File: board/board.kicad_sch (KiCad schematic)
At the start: 5 parts, among them J1 022_battery_cells, J2 Conn_01x02_Male, J3 003_power

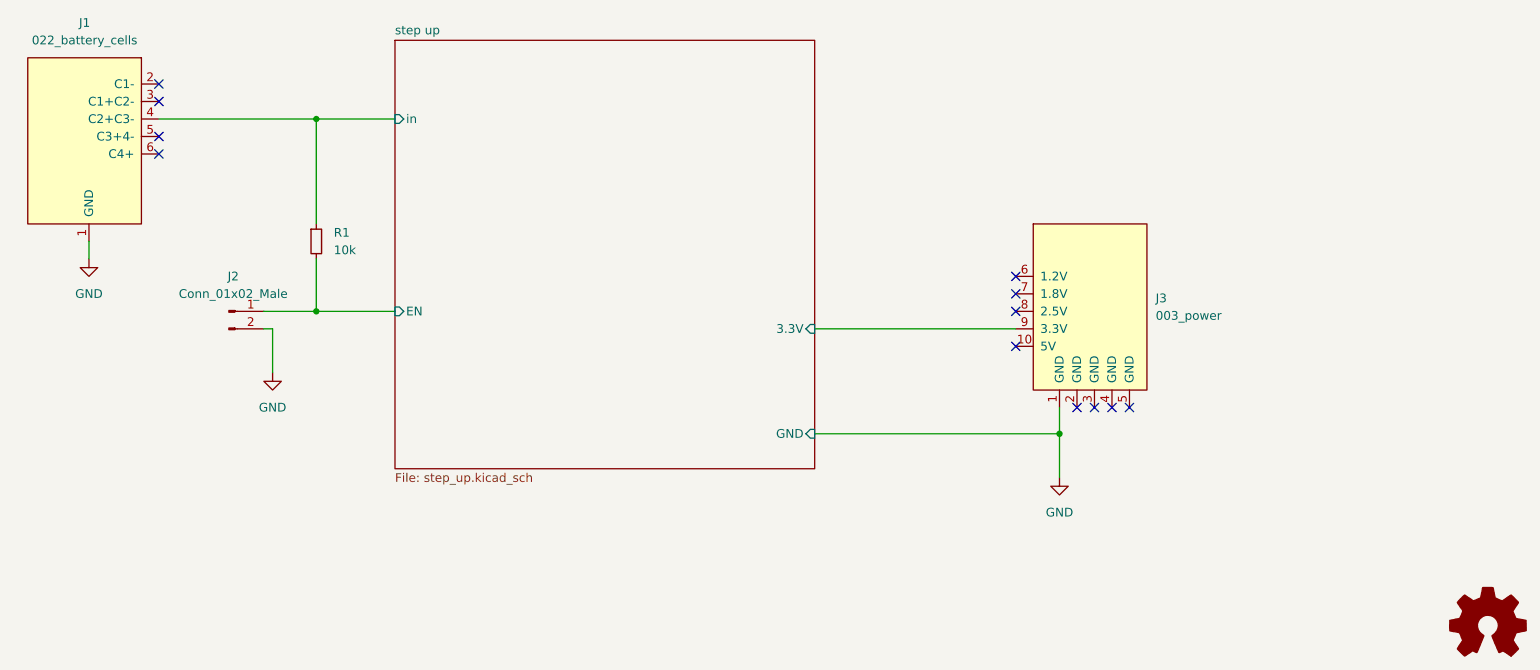
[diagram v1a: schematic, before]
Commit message: added resistor to allow shorting of bat low to gnd
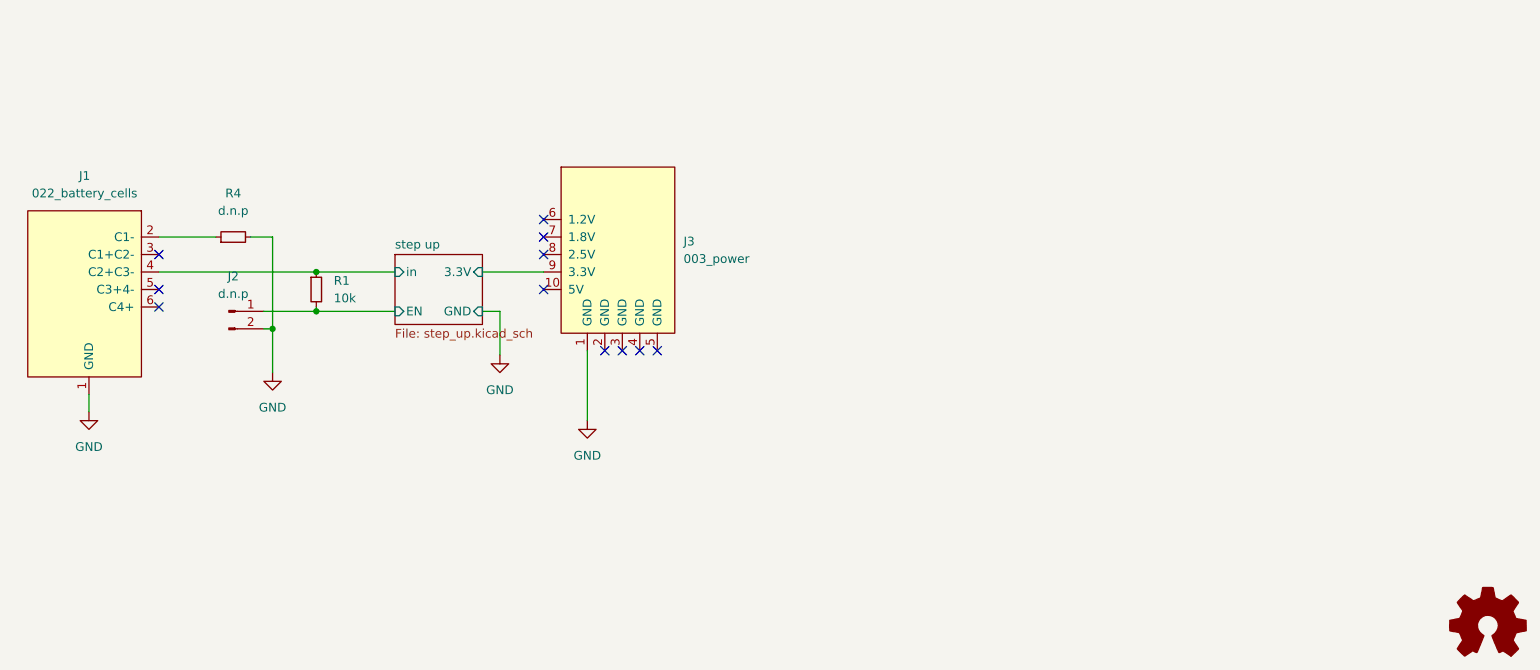
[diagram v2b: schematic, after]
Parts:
- added R4: d.n.p, Resistor_SMD:R_0603_1608Metric, symbol Device:R_Small
- J2: value Conn_01x02_Male -> d.n.p
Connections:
- net GND: now also R4.2
- net at J1.2 (C1-): now also R4.1
- no-connect marks 12 -> 11
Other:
- moved on the sheet: J1, J3, R1
